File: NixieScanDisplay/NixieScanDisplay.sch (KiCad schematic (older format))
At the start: 104 parts, among them J1 Conn_01x07, J2 Conn_01x01, J3 Conn_01x01, J4 Conn_01x01, J5 Conn_01x01, Q1 2N2222A, Q10 MPSA42, Q11 MPSA42, Q12 MPSA42, Q13 MPSA42, Q14 MPSA42, Q15 MPSA92, Q16 MPSA42, Q17 MPSA42, Q18 MPSA92, Q19 MPSA42, Q2 IRF840, Q20 MPSA42, Q21 MPSA42, Q22 MPSA92, Q23 MPSA42, Q24 MPSA92, Q25 MPSA42, Q26 MPSA92, Q3 MPSA42, Q4 MPSA42, Q5 MPSA42, Q6 MPSA42, Q7 MPSA92, Q8 MPSA42, Q9 MPSA42, U1 NE555, U2 L7805, U3 74HC595, U4 74HC595, U5 74HC595

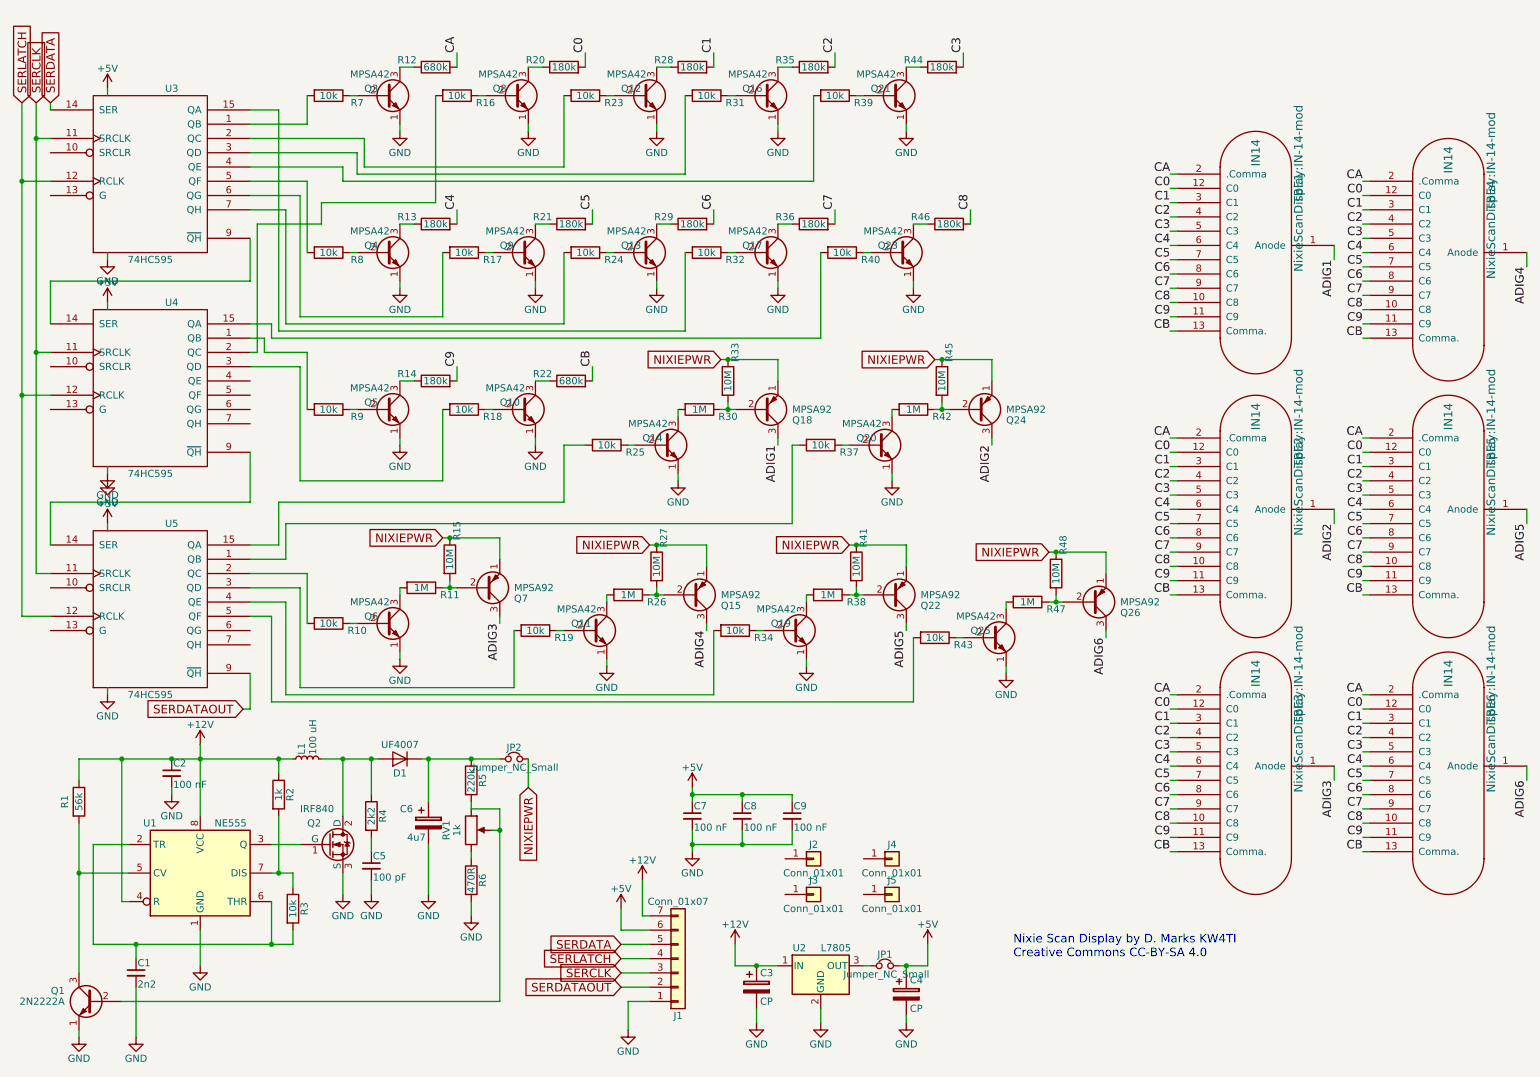
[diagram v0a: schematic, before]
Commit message: First usable version of Nixie Tube Clock
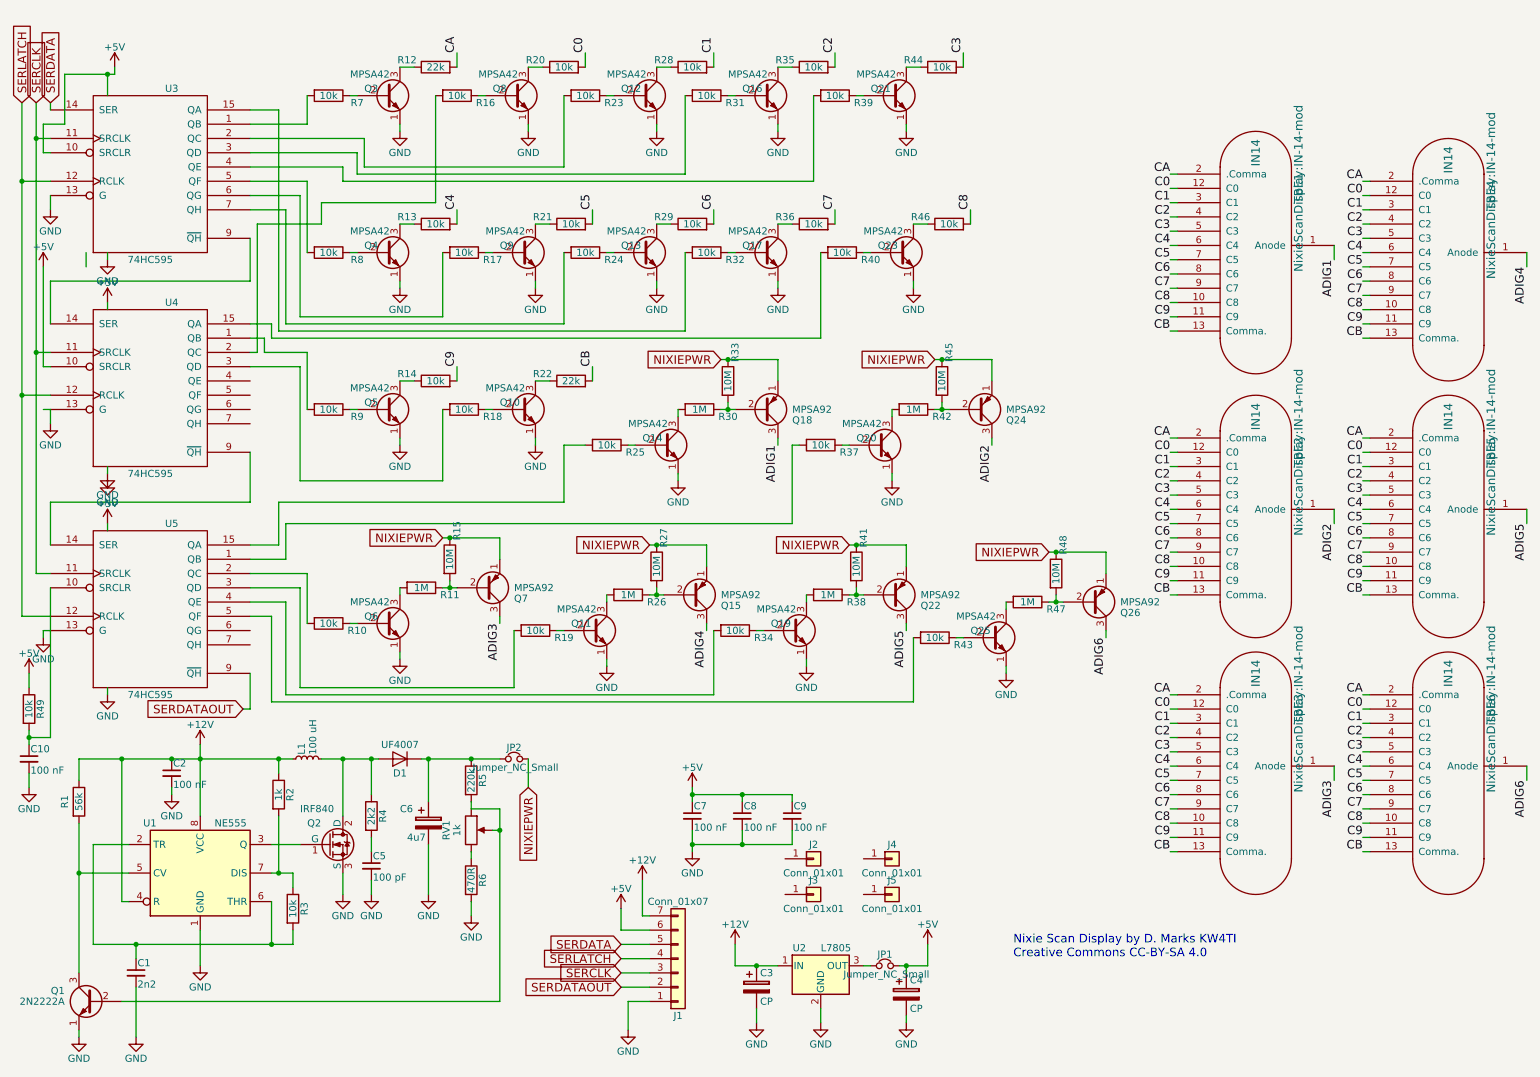
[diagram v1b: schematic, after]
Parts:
- added C10: 100 nF, Capacitors_THT:C_Disc_D5.0mm_W2.5mm_P2.50mm, symbol C_Small
- added R49: 10k, Resistors_THT:R_Axial_DIN0207_L6.3mm_D2.5mm_P7.62mm_Horizontal, symbol R
- C6: footprint Capacitors_THT:CP_Radial_D8.0mm_P3.50mm -> Capacitors_THT:CP_Radial_D14.0mm_P7.50mm
- R12, R22: value 680k -> 22k
- R13, R14, R20, R21, R28, R29, R35, R36, R44, R46: value 180k -> 10k
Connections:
- net +5V: now also U3.10 (SRCLR), U4.10 (SRCLR), R49.1
- net GND: now also U3.13 (G), U4.13 (G), U5.13 (G), C10.2
- net at U5.10 (SRCLR): now also C10.1, R49.2
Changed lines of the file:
@@
 F 0 "C6" H 3200 6100 50  0000 L CNN
 F 1 "4u7" H 3250 5900 50  0000 L CNN
-F 2 "Capacitors_THT:CP_Radial_D8.0mm_P3.50mm" H 3438 5850 50  0001 C CNN
+F 2 "Capacitors_THT:CP_Radial_D14.0mm_P7.50mm" H 3438 5850 50  0001 C CNN
 F 3 "" H 3400 6000 50  0001 C CNN
 	1    3400 6000
@@
 $EndComp
 $Comp
-L 74HC595 U3
-U 1 1 5E0B62BC
-P 1450 1450
-F 0 "U3" H 1600 2050 50  0000 C CNN
-F 1 "74HC595" H 1450 850 50  0000 C CNN
-F 2 "Housings_DIP:DIP-16_W7.62mm_Socket" H 1450 1450 50  0001 C CNN
-F 3 "" H 1450 1450 50  0001 C CNN
-	1    1450 1450
-	1    0    0    -1
-$EndComp
-$Comp
 L R R12
 U 1 1 5E0B62C3
 P 3450 700
 F 0 "R12" V 3500 900 50  0000 C CNN
-F 1 "680k" V 3450 700 50  0000 C CNN
+F 1 "22k" V 3450 700 50  0000 C CNN
 F 2 "Resistors_THT:R_Axial_DIN0207_L6.3mm_D2.5mm_P7.62mm_Horizontal" V 3380 700 50  0001 C CNN
 F 3 "" H 3450 700 50  0001 C CNN
@@
 L +5V #PWR020
 U 1 1 5E0BCE95
-P 1150 850
-F 0 "#PWR020" H 1150 700 50  0001 C CNN
-F 1 "+5V" H 1150 990 50  0000 C CNN
-F 2 "" H 1150 850 50  0001 C CNN
-F 3 "" H 1150 850 50  0001 C CNN
-	1    1150 850
+P 1200 700
+F 0 "#PWR020" H 1200 550 50  0001 C CNN
+F 1 "+5V" H 1200 840 50  0000 C CNN
+F 2 "" H 1200 700 50  0001 C CNN
+F 3 "" H 1200 700 50  0001 C CNN
+	1    1200 700
 	1    0    0    -1
 $EndComp
@@
 $EndComp
 $Comp
-L 74HC595 U4
-U 1 1 5E0BF082
-P 1450 2950
-F 0 "U4" H 1600 3550 50  0000 C CNN
-F 1 "74HC595" H 1450 2350 50  0000 C CNN
-F 2 "Housings_DIP:DIP-16_W7.62mm_Socket" H 1450 2950 50  0001 C CNN
-F 3 "" H 1450 2950 50  0001 C CNN
-	1    1450 2950
-	1    0    0    -1
-$EndComp
-$Comp
 L +5V #PWR022
 U 1 1 5E0BF288
@@
 P 4350 700
 F 0 "R20" V 4400 900 50  0000 C CNN
-F 1 "180k" V 4350 700 50  0000 C CNN
+F 1 "10k" V 4350 700 50  0000 C CNN
 F 2 "Resistors_THT:R_Axial_DIN0207_L6.3mm_D2.5mm_P7.62mm_Horizontal" V 4280 700 50  0001 C CNN
 F 3 "" H 4350 700 50  0001 C CNN
@@
 P 5250 700
 F 0 "R28" V 5300 900 50  0000 C CNN
-F 1 "180k" V 5250 700 50  0000 C CNN
+F 1 "10k" V 5250 700 50  0000 C CNN
 F 2 "Resistors_THT:R_Axial_DIN0207_L6.3mm_D2.5mm_P7.62mm_Horizontal" V 5180 700 50  0001 C CNN
 F 3 "" H 5250 700 50  0001 C CNN
@@
 P 6100 700
 F 0 "R35" V 6150 900 50  0000 C CNN
-F 1 "180k" V 6100 700 50  0000 C CNN
+F 1 "10k" V 6100 700 50  0000 C CNN
 F 2 "Resistors_THT:R_Axial_DIN0207_L6.3mm_D2.5mm_P7.62mm_Horizontal" V 6030 700 50  0001 C CNN
 F 3 "" H 6100 700 50  0001 C CNN
@@
 P 7000 700
 F 0 "R44" V 7050 900 50  0000 C CNN
-F 1 "180k" V 7000 700 50  0000 C CNN
+F 1 "10k" V 7000 700 50  0000 C CNN
 F 2 "Resistors_THT:R_Axial_DIN0207_L6.3mm_D2.5mm_P7.62mm_Horizontal" V 6930 700 50  0001 C CNN
 F 3 "" H 7000 700 50  0001 C CNN
@@
 P 3450 1800
 F 0 "R13" V 3500 2000 50  0000 C CNN
-F 1 "180k" V 3450 1800 50  0000 C CNN
+F 1 "10k" V 3450 1800 50  0000 C CNN
 F 2 "Resistors_THT:R_Axial_DIN0207_L6.3mm_D2.5mm_P7.62mm_Horizontal" V 3380 1800 50  0001 C CNN
 F 3 "" H 3450 1800 50  0001 C CNN
@@
 P 4400 1800
 F 0 "R21" V 4450 2000 50  0000 C CNN
-F 1 "180k" V 4400 1800 50  0000 C CNN
+F 1 "10k" V 4400 1800 50  0000 C CNN
 F 2 "Resistors_THT:R_Axial_DIN0207_L6.3mm_D2.5mm_P7.62mm_Horizontal" V 4330 1800 50  0001 C CNN
 F 3 "" H 4400 1800 50  0001 C CNN
@@
 P 5250 1800
 F 0 "R29" V 5300 2000 50  0000 C CNN
-F 1 "180k" V 5250 1800 50  0000 C CNN
+F 1 "10k" V 5250 1800 50  0000 C CNN
 F 2 "Resistors_THT:R_Axial_DIN0207_L6.3mm_D2.5mm_P7.62mm_Horizontal" V 5180 1800 50  0001 C CNN
 F 3 "" H 5250 1800 50  0001 C CNN
@@
 P 6100 1800
 F 0 "R36" V 6150 2000 50  0000 C CNN
-F 1 "180k" V 6100 1800 50  0000 C CNN
+F 1 "10k" V 6100 1800 50  0000 C CNN
 F 2 "Resistors_THT:R_Axial_DIN0207_L6.3mm_D2.5mm_P7.62mm_Horizontal" V 6030 1800 50  0001 C CNN
 F 3 "" H 6100 1800 50  0001 C CNN
@@
 P 7050 1800
 F 0 "R46" V 7100 2000 50  0000 C CNN
-F 1 "180k" V 7050 1800 50  0000 C CNN
+F 1 "10k" V 7050 1800 50  0000 C CNN
 F 2 "Resistors_THT:R_Axial_DIN0207_L6.3mm_D2.5mm_P7.62mm_Horizontal" V 6980 1800 50  0001 C CNN
 F 3 "" H 7050 1800 50  0001 C CNN
@@
 P 3450 2900
 F 0 "R14" V 3500 3100 50  0000 C CNN
-F 1 "180k" V 3450 2900 50  0000 C CNN
+F 1 "10k" V 3450 2900 50  0000 C CNN
 F 2 "Resistors_THT:R_Axial_DIN0207_L6.3mm_D2.5mm_P7.62mm_Horizontal" V 3380 2900 50  0001 C CNN
 F 3 "" H 3450 2900 50  0001 C CNN
@@
 P 4400 2900
 F 0 "R22" V 4450 3100 50  0000 C CNN
-F 1 "680k" V 4400 2900 50  0000 C CNN
+F 1 "22k" V 4400 2900 50  0000 C CNN
 F 2 "Resistors_THT:R_Axial_DIN0207_L6.3mm_D2.5mm_P7.62mm_Horizontal" V 4330 2900 50  0001 C CNN
 F 3 "" H 4400 2900 50  0001 C CNN
@@
 Text Label 8150 4700 3    60   ~ 0
 ADIG6
+Text Notes 7500 6950 0    60   ~ 0
+Nixie Scan Display by D. Marks KW4TI\nCreative Commons CC-BY-SA 4.0
+$Comp
+L GND #PWR045
+U 1 1 5E52AC37
+P 700 4700
+F 0 "#PWR045" H 700 4450 50  0001 C CNN
+F 1 "GND" H 700 4550 50  0000 C CNN
+F 2 "" H 700 4700 50  0001 C CNN
+F 3 "" H 700 4700 50  0001 C CNN
+	1    700  4700
+	1    0    0    -1
+$EndComp
 Wire Wire Line
 	4800 7450 4800 7250
@@
 	750  950  750  1000
 Wire Wire Line
-	650  950  650  4250
-Wire Wire Line
 	650  1200 750  1200
 Wire Wire Line
@@
 Connection ~ 5600 5800
 Wire Wire Line
-	1150 850  1150 900
+	1150 750  1150 900
 Wire Wire Line
 	1150 2050 1150 2000
@@
 Wire Wire Line
 	2550 1100 2550 900
-Text Notes 7500 6950 0    60   ~ 0
-Nixie Scan Display by D. Marks KW4TI\nCreative Commons CC-BY-SA 4.0
+Wire Wire Line
+	700  4700 700  4650
+Wire Wire Line
+	700  4650 750  4650
+Wire Wire Line
+	750  3200 750  3100
+$Comp
+L GND #PWR046
+U 1 1 5E52BBCD
+P 750 1700
+F 0 "#PWR046" H 750 1450 50  0001 C CNN
+F 1 "GND" H 750 1550 50  0000 C CNN
+F 2 "" H 750 1700 50  0001 C CNN
+F 3 "" H 750 1700 50  0001 C CNN
+	1    750  1700
+	1    0    0    -1
+$EndComp
+Wire Wire Line
+	750  1700 750  1600
+Wire Wire Line
+	750  4350 750  5400
+$Comp
+L C_Small C10
+U 1 1 5E54B9DD
+P 600 5550
+F 0 "C10" H 610 5620 50  0000 L CNN
+F 1 "100 nF" H 610 5470 50  0000 L CNN
+F 2 "Capacitors_THT:C_Disc_D5.0mm_W2.5mm_P2.50mm" H 600 5550 50  0001 C CNN
+F 3 "" H 600 5550 50  0001 C CNN
+	1    600  5550
+	1    0    0    -1
+$EndComp
+$Comp
+L GND #PWR047
+U 1 1 5E54C09E
+P 600 5750
+F 0 "#PWR047" H 600 5500 50  0001 C CNN
+F 1 "GND" H 600 5600 50  0000 C CNN
+F 2 "" H 600 5750 50  0001 C CNN
+F 3 "" H 600 5750 50  0001 C CNN
+	1    600  5750
+	1    0    0    -1
+$EndComp
+Wire Wire Line
+	600  5650 600  5750
+$Comp
+L R R49
+U 1 1 5E54C4A9
+P 600 5200
+F 0 "R49" V 680 5200 50  0000 C CNN
+F 1 "10k" V 600 5200 50  0000 C CNN
+F 2 "Resistors_THT:R_Axial_DIN0207_L6.3mm_D2.5mm_P7.62mm_Horizontal" V 530 5200 50  0001 C CNN
+F 3 "" H 600 5200 50  0001 C CNN
+	1    600  5200
+	1    0    0    -1
+$EndComp
+Wire Wire Line
+	600  5350 600  5450
+$Comp
+L +5V #PWR048
+U 1 1 5E54CAE2
+P 600 4950
+F 0 "#PWR048" H 600 4800 50  0001 C CNN
+F 1 "+5V" H 600 5090 50  0000 C CNN
+F 2 "" H 600 4950 50  0001 C CNN
+F 3 "" H 600 4950 50  0001 C CNN
+	1    600  4950
+	1    0    0    -1
+$EndComp
+Wire Wire Line
+	600  5050 600  4950
+Wire Wire Line
+	750  5400 600  5400
+Connection ~ 600  5400
+Wire Wire Line
+	750  1300 700  1300
+Wire Wire Line
+	750  3100 700  3100
+$Comp
+L +5V #PWR049
+U 1 1 5E54F6E9
+P 700 2100
+F 0 "#PWR049" H 700 1950 50  0001 C CNN
+F 1 "+5V" H 700 2240 50  0000 C CNN
+F 2 "" H 700 2100 50  0001 C CNN
+F 3 "" H 700 2100 50  0001 C CNN
+	1    700  2100
+	1    0    0    -1
+$EndComp
+Wire Wire Line
+	1200 750  1200 700
+Wire Wire Line
+	850  750  1200 750
+Wire Wire Line
+	850  750  850  1100
+Wire Wire Line
+	850  1100 700  1100
+Wire Wire Line
+	1000 2000 1000 2100
+$Comp
+L 74HC595 U4
+U 1 1 5E0BF082
+P 1450 2950
+F 0 "U4" H 1600 3550 50  0000 C CNN
+F 1 "74HC595" H 1450 2350 50  0000 C CNN
+F 2 "Housings_DIP:DIP-16_W7.62mm_Socket" H 1450 2950 50  0001 C CNN
+F 3 "" H 1450 2950 50  0001 C CNN
+	1    1450 2950
+	1    0    0    -1
+$EndComp
+$Comp
+L GND #PWR050
+U 1 1 5E52B098
+P 750 3200
+F 0 "#PWR050" H 750 2950 50  0001 C CNN
+F 1 "GND" H 750 3050 50  0000 C CNN
+F 2 "" H 750 3200 50  0001 C CNN
+F 3 "" H 750 3200 50  0001 C CNN
+	1    750  3200
+	1    0    0    -1
+$EndComp
+Wire Wire Line
+	700  2100 700  2800
+Wire Wire Line
+	700  2800 750  2800
+Connection ~ 1150 750
+$Comp
+L 74HC595 U3
+U 1 1 5E0B62BC
+P 1450 1450
+F 0 "U3" H 1600 2050 50  0000 C CNN
+F 1 "74HC595" H 1450 850 50  0000 C CNN
+F 2 "Housings_DIP:DIP-16_W7.62mm_Socket" H 1450 1450 50  0001 C CNN
+F 3 "" H 1450 1450 50  0001 C CNN
+	1    1450 1450
+	1    0    0    -1
+$EndComp
+Wire Wire Line
+	650  950  650  4250
+Wire Wire Line
+	700  1100 700  1300
 $EndSCHEMATC

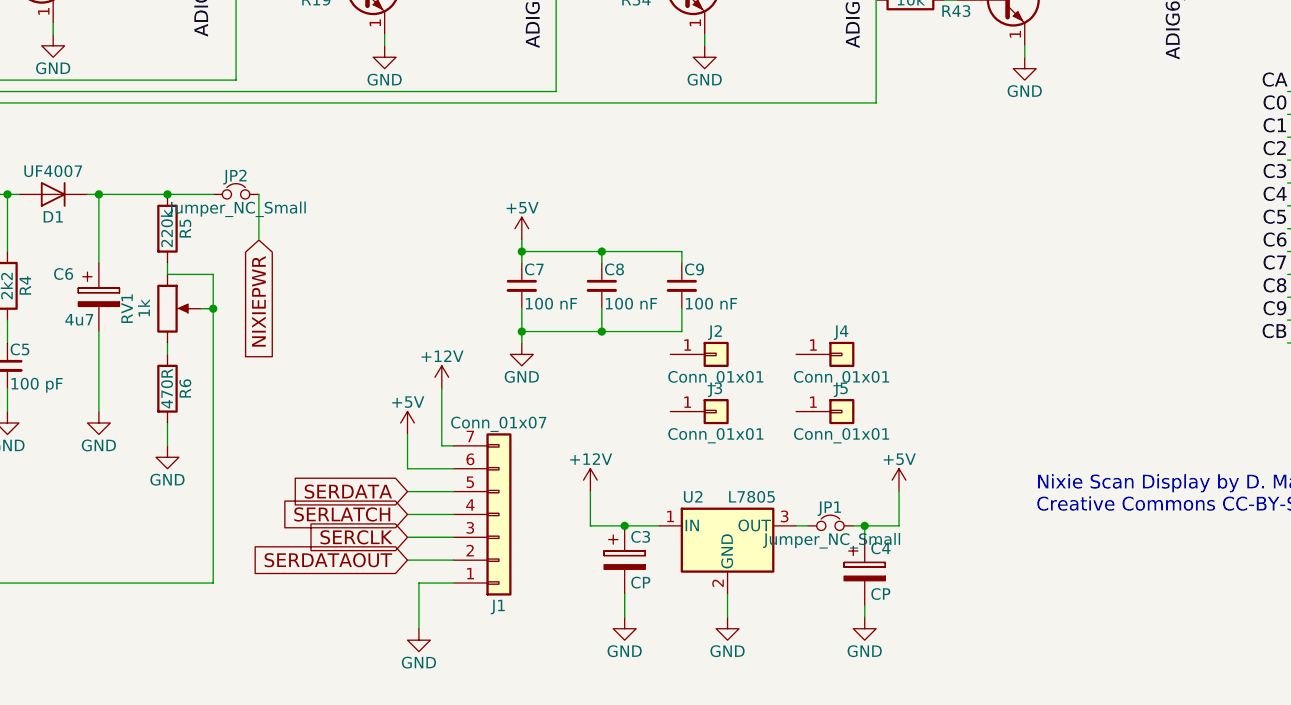
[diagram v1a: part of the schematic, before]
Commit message: Changed connector between boards to 10 pin IDC, added Bill of Materials
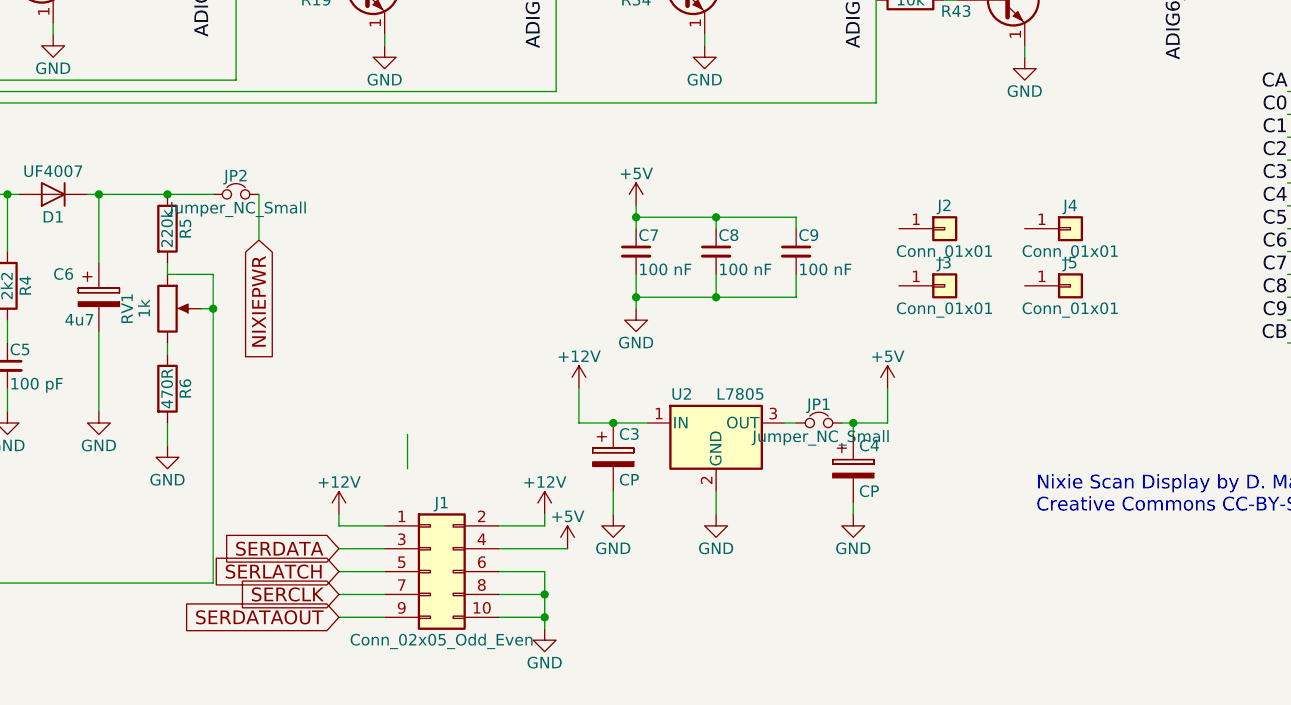
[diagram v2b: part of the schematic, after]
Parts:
- removed J1: Conn_01x07, Connectors_Molex:Molex_KK-6410-07_07x2.54mm_Straight, symbol Conn_01x07
- added J1: Conn_02x05_Odd_Even, Pin_Headers:Pin_Header_Straight_2x05_Pitch2.54mm, symbol Conn_02x05_Odd_Even
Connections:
- net +12V: now also J1.1 (Pin_1), J1.2 (Pin_2)
- net +5V: now also J1.4 (Pin_4)
- net GND: now also J1.10 (Pin_10), J1.6 (Pin_6), J1.8 (Pin_8)
- net SERCLK: now also J1.7 (Pin_7)
- net SERDATA: now also J1.3 (Pin_3)
- net SERDATAOUT: now also J1.9 (Pin_9)
- net SERLATCH: now also J1.5 (Pin_5)
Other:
- moved on the sheet: C3, C4, C7, C8, C9, J2, J3, J4, J5, JP1, U2
